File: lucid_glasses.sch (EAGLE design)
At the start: 7 parts, among them IC1 AT90LS2343P, IC2 786TV

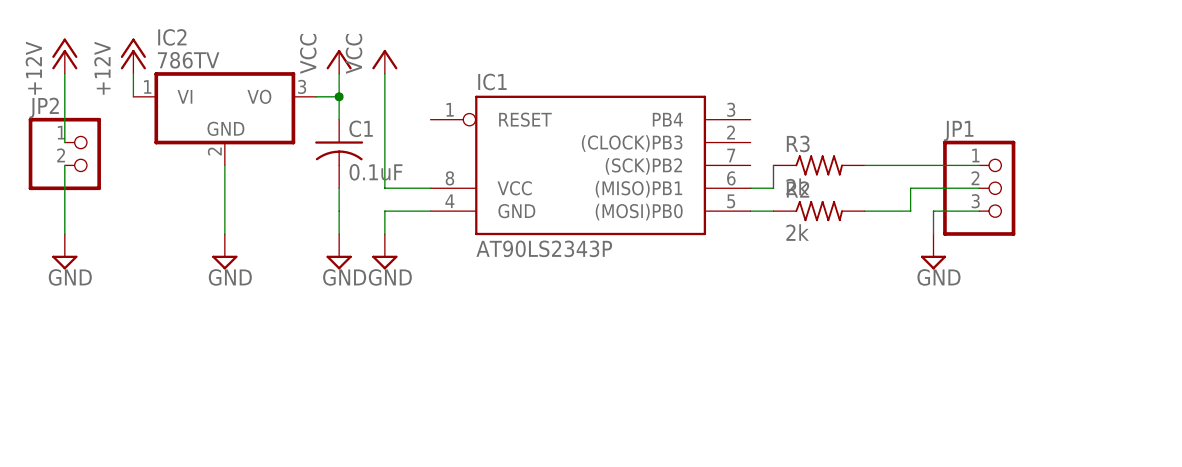
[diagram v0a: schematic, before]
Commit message: Updated board for smt with coin cell battery.
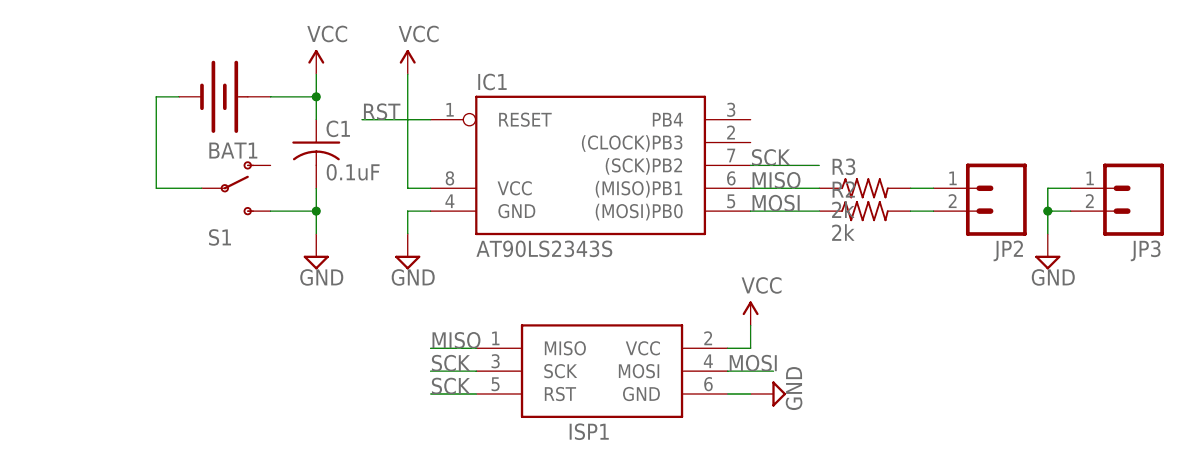
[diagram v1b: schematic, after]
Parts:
- removed IC2: 786TV, linear:786TV
- removed JP1: (no value), adafruit:PINHD-1X3
- added BAT1: (no value), sparkfun:BATTERY20SMD
- added ISP1: AVRISP-6, adafruit:AVRISP-6
- added JP3: (no value), sparkfun:M02PTH
- added S1: (no value), sparkfun:SWITCH-SPSTSMD2
- C1: device adafruit:C-US025-024X044 -> adafruit:C-USC1206
- IC1: value AT90LS2343P -> AT90LS2343S; device atmel:AT90LS2343P -> atmel:AT90LS2343S
- JP2: device pinhead:PINHD-1X2 -> sparkfun:M02PTH
- R2, R3: device resistor:R-US_0309/V -> resistor:R-US_R1206
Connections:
- removed net +12V: IC2.VI, JP2.1
- removed net N$3: IC1.(MISO)PB1, R3.1
- new net MISO: IC1.(MISO)PB1, ISP1.MISO, R3.1
- new net MOSI: IC1.(MOSI)PB0, ISP1.MOSI, R2.1
- new net RST: IC1.RESET, ISP1.RST
- new net SCK: IC1.(SCK)PB2, ISP1.SCK
- net GND: now also ISP1.GND, JP3.1, JP3.2, S1.S; no longer IC2.GND, JP1.3, JP2.2
- net N$1: now also JP2.1; no longer JP1.1
- net N$2: now also BAT1.-, S1.P; no longer IC1.(MOSI)PB0, R2.1
- net N$4: now also JP2.2; no longer JP1.2
- net VCC: now also BAT1.+, ISP1.VCC; no longer IC2.VO
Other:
- moved on the sheet: C1, JP2, R2, R3
